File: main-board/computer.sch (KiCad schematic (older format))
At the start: 17 parts, among them J1 Expansion, J2 Expansion, SW1 RESET, U1 W65C02SxP, U2 28C256, U3 AS6C62256, U4 74HC00, U5 DS1813, X1 1MHz

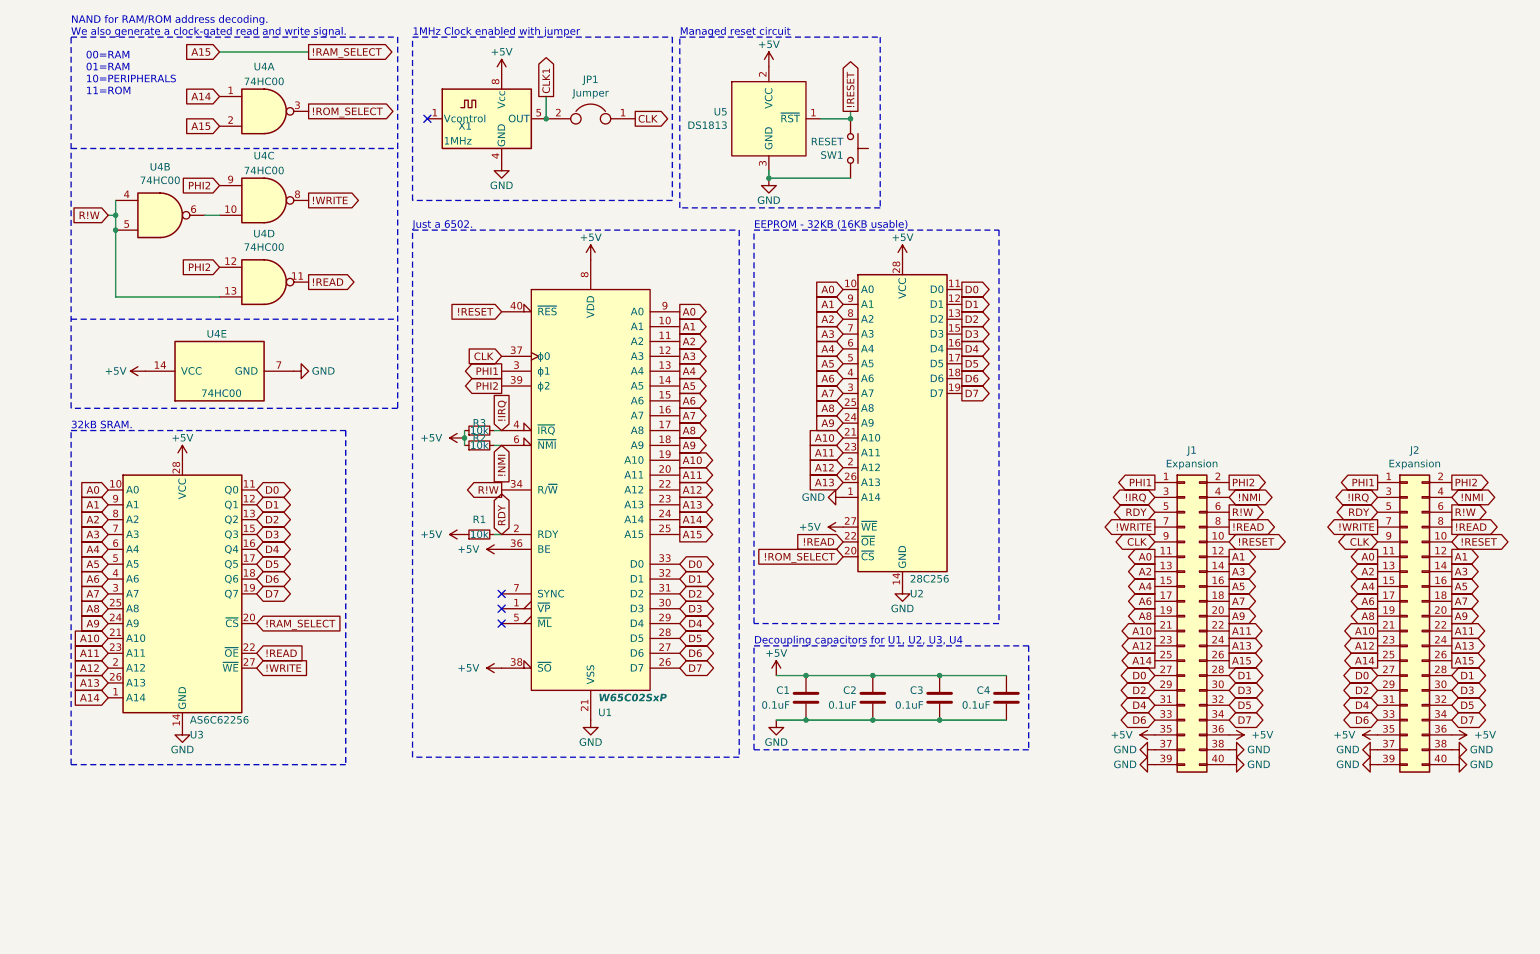
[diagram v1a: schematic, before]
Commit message: remove vga board, finish other boards
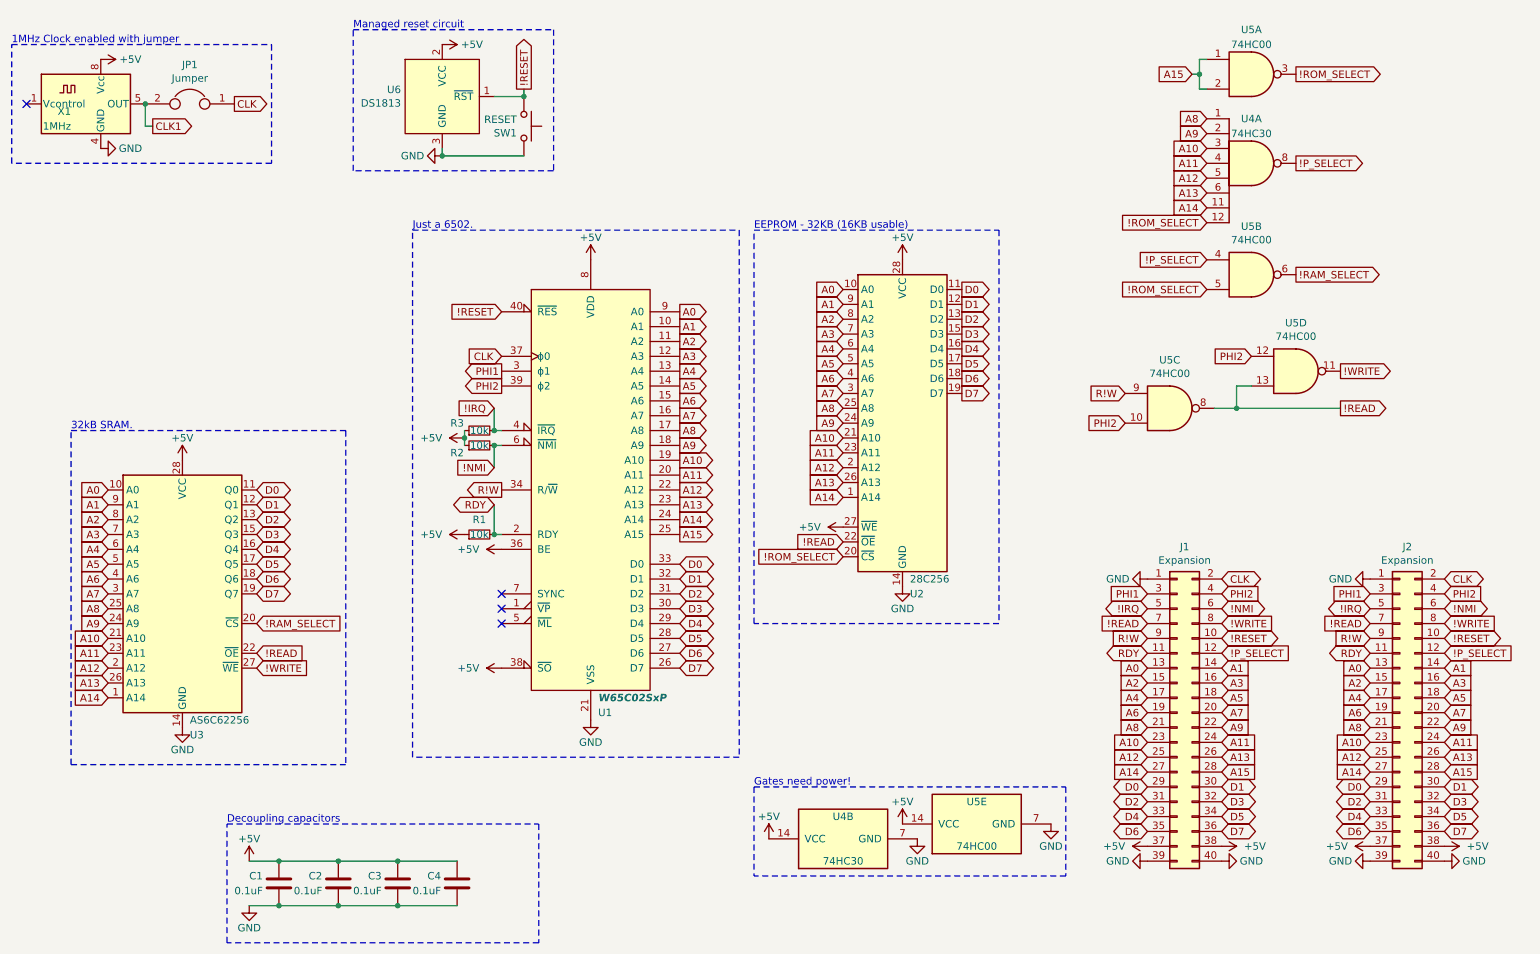
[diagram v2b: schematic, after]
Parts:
- removed U4: 74HC00, Package_DIP:DIP-14_W7.62mm_Socket, symbol 74xx:74HC00
- added U4: 74HC30, Package_DIP:DIP-14_W7.62mm_Socket, symbol 74xx:74LS30
- added U5: 74HC00, Package_DIP:DIP-14_W7.62mm_Socket, symbol 74xx:74HC00
- renumbered U5 to U6
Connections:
- net !IRQ: now also J1.5 (Pin_5), J2.5 (Pin_5); no longer J1.3 (Pin_3), J2.3 (Pin_3)
- net !NMI: now also J1.6 (Pin_6), J2.6 (Pin_6); no longer J1.4 (Pin_4), J2.4 (Pin_4)
- net !RAM_SELECT: now also U5.6; no longer J1.26 (Pin_26), J2.26 (Pin_26), U1.25 (A15)
- net !READ: now also J1.7 (Pin_7), J2.7 (Pin_7), U5.13, U5.8; no longer J1.8 (Pin_8), J2.8 (Pin_8)
- net !ROM_SELECT: now also U4.12, U5.3, U5.5
- net !WRITE: now also J1.8 (Pin_8), J2.8 (Pin_8), U5.11; no longer J1.7 (Pin_7), J2.7 (Pin_7)
- net +5V: now also J1.37 (Pin_37), J1.38 (Pin_38), J2.37 (Pin_37), J2.38 (Pin_38), U4.14 (VCC), U5.14 (VCC); no longer J1.35 (Pin_35), J1.36 (Pin_36), J2.35 (Pin_35), J2.36 (Pin_36)
- net A0: now also J1.13 (Pin_13), J2.13 (Pin_13); no longer J1.11 (Pin_11), J2.11 (Pin_11)
- net A1: now also J1.14 (Pin_14), J2.14 (Pin_14); no longer J1.12 (Pin_12), J2.12 (Pin_12)
- net A10: now also J1.23 (Pin_23), J2.23 (Pin_23), U4.3; no longer J1.21 (Pin_21), J2.21 (Pin_21)
- net A11: now also J1.24 (Pin_24), J2.24 (Pin_24), U4.4; no longer J1.22 (Pin_22), J2.22 (Pin_22)
- net A12: now also J1.25 (Pin_25), J2.25 (Pin_25), U4.5; no longer J1.23 (Pin_23), J2.23 (Pin_23)
- net A13: now also J1.26 (Pin_26), J2.26 (Pin_26), U4.6; no longer J1.24 (Pin_24), J2.24 (Pin_24)
- net A14: now also J1.27 (Pin_27), J2.27 (Pin_27), U2.1 (A14), U4.11; no longer J1.25 (Pin_25), J2.25 (Pin_25)
- net A2: now also J1.15 (Pin_15), J2.15 (Pin_15); no longer J1.13 (Pin_13), J2.13 (Pin_13)
- net A3: now also J1.16 (Pin_16), J2.16 (Pin_16); no longer J1.14 (Pin_14), J2.14 (Pin_14)
- net A4: now also J1.17 (Pin_17), J2.17 (Pin_17); no longer J1.15 (Pin_15), J2.15 (Pin_15)
- net A5: now also J1.18 (Pin_18), J2.18 (Pin_18); no longer J1.16 (Pin_16), J2.16 (Pin_16)
- net A6: now also J1.19 (Pin_19), J2.19 (Pin_19); no longer J1.17 (Pin_17), J2.17 (Pin_17)
- net A7: now also J1.20 (Pin_20), J2.20 (Pin_20); no longer J1.18 (Pin_18), J2.18 (Pin_18)
- net A8: now also J1.21 (Pin_21), J2.21 (Pin_21), U4.1; no longer J1.19 (Pin_19), J2.19 (Pin_19)
- net A9: now also J1.22 (Pin_22), J2.22 (Pin_22), U4.2; no longer J1.20 (Pin_20), J2.20 (Pin_20)
- net CLK: now also J1.2 (Pin_2), J2.2 (Pin_2); no longer J1.9 (Pin_9), J2.9 (Pin_9)
- net D0: now also J1.29 (Pin_29), J2.29 (Pin_29); no longer J1.27 (Pin_27), J2.27 (Pin_27)
- net D1: now also J1.30 (Pin_30), J2.30 (Pin_30); no longer J1.28 (Pin_28), J2.28 (Pin_28)
- net D2: now also J1.31 (Pin_31), J2.31 (Pin_31); no longer J1.29 (Pin_29), J2.29 (Pin_29)
- net D3: now also J1.32 (Pin_32), J2.32 (Pin_32); no longer J1.30 (Pin_30), J2.30 (Pin_30)
- net D4: now also J1.33 (Pin_33), J2.33 (Pin_33); no longer J1.31 (Pin_31), J2.31 (Pin_31)
- net D5: now also J1.34 (Pin_34), J2.34 (Pin_34); no longer J1.32 (Pin_32), J2.32 (Pin_32)
- net D6: now also J1.35 (Pin_35), J2.35 (Pin_35); no longer J1.33 (Pin_33), J2.33 (Pin_33)
- net D7: now also J1.36 (Pin_36), J2.36 (Pin_36); no longer J1.34 (Pin_34), J2.34 (Pin_34)
- net GND: now also J1.1 (Pin_1), J2.1 (Pin_1), U4.7 (GND), U5.7 (GND); no longer J1.37 (Pin_37), J1.38 (Pin_38), J2.37 (Pin_37), J2.38 (Pin_38), U2.1 (A14)
- net PHI1: now also J1.3 (Pin_3), J2.3 (Pin_3); no longer J1.1 (Pin_1), J2.1 (Pin_1)
- net PHI2: now also J1.4 (Pin_4), J2.4 (Pin_4), U5.10, U5.12; no longer J1.2 (Pin_2), J2.2 (Pin_2)
- net R!W: now also J1.9 (Pin_9), J2.9 (Pin_9), U5.9; no longer J1.6 (Pin_6), J2.6 (Pin_6)
- net RDY: now also J1.11 (Pin_11), J2.11 (Pin_11); no longer J1.5 (Pin_5), J2.5 (Pin_5)
- new net !P_SELECT: J1.12 (Pin_12), J2.12 (Pin_12), U4.8, U5.4
- new net A15: J1.28 (Pin_28), J2.28 (Pin_28), U1.25 (A15), U5.1, U5.2
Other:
- note added: "Decoupling capacitors"
- note added: "Gates need power!"
- note removed: "Decoupling capacitors for U1, U2, U3, U4"
- note removed: "NAND for RAM/ROM address decoding.\nWe also generate a clock-gated read and write signal."
- note removed: "\n00=RAM\n01=RAM\n10=PERIPHERALS\n11=ROM"
- moved on the sheet: C1, C2, C3, C4, J1, JP1, SW1, U6, X1
